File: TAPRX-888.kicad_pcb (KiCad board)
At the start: 6 copper layers, 76 x 100 mm, 222 parts, among them J1 CONN_SMA_JACK_RA, J10 U.FL-R, J11 Conn_JTAG10-mini, J2 CONN_SMA_JACK_RA, J3 CONN_SMA_JACK_RA, J4 CONN_SMA_JACK_RA, J5 USB-3.0, J6 Conn_01x03, J7 Conn_01x03, J8 Conn_01x03, J9 Conn_01x03, Q1 PMOS Si2343DS, Q2 MMBT3904, Q3 PMOS Si2343DS, U1 AP2114H-3.3TRG1, U10 XO-19.2MHZ, U11 CYUSB3014-BZXCT, U14 LP5907MFX-3.3, U16 TLV3501, U18 NC7SV157, U19 74LVC2G14, U2 AP2114H-3.3TRG1, U20 Si5351A, U21 NC7SV157, U22 SN65LVDS1, U3 AP2114H-3.3TRG1, U4 LP5907MFX-3.3, U5 UMW AMS1117-1.2, U6 AD8370, U7 TVS-SP3011, U8 LTC2208CUP_PBF, U9 MX25L3233FM2I, X1 TCXO-27M

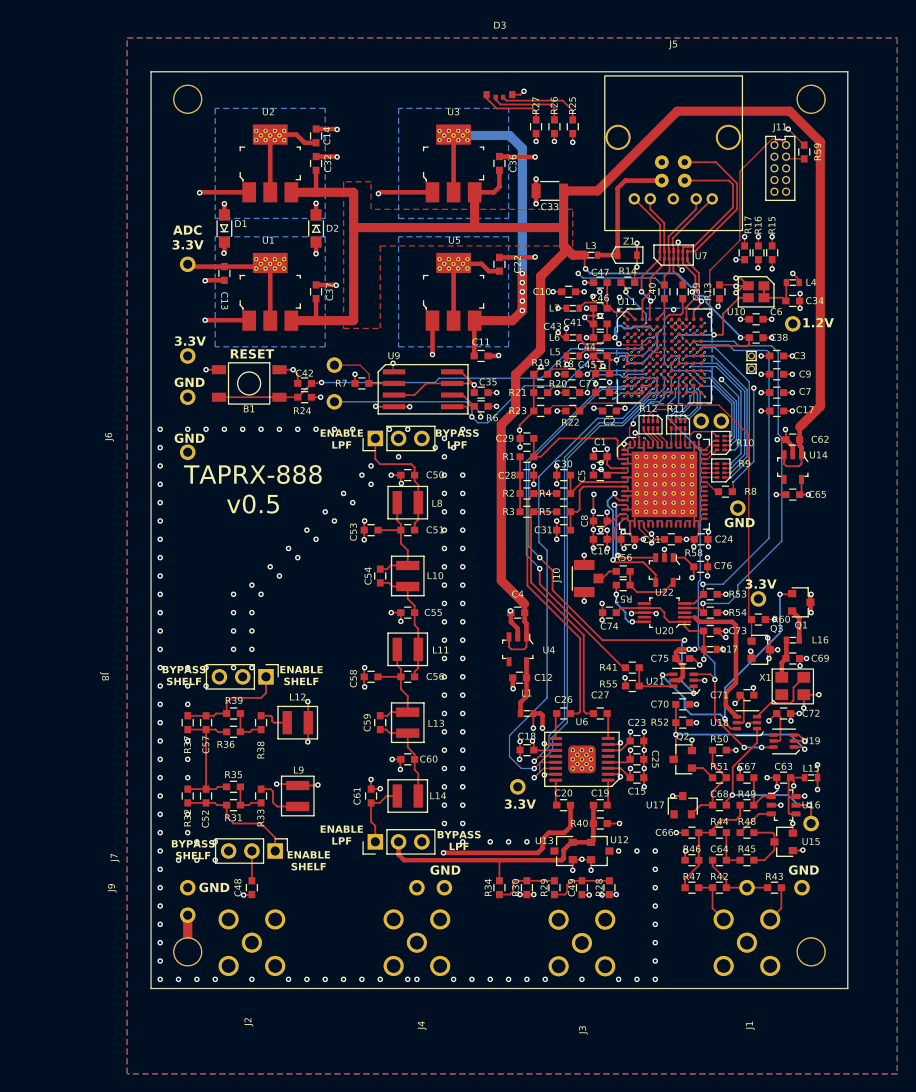
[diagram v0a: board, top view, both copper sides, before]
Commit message: Swap in newest design from TAPR/TAPRx888 c01bece; re-graft repo infra
The authoritative HF-SDR design was updated by the hardware designer on
TAPR/TAPRx888 (commit c01bece "proper update", Turn Island Systems). That
branch sits on the pre-flatten layout and also carried a stray
"TAPRX-888 KiCad - Copy/" duplicate + editor lock files, so a plain
cherry-pick was impossible. This lands only the real design edits, mapped
onto ringof's flattened root, and re-applies ringof's infra on top.

Design content taken verbatim from c01bece (mapped to repo root):
  - TAPRX-888.kicad_pcb   (layout/routing/net updates)
  - TAPRX-888.kicad_sch   (root schematic)
  - refclk.kicad_sch      (reference-clock sheet)
  - Library.kicad_sym     (symbol tweak)
  - TAPRX-888.kicad_pro   (used_designators, GIT_HASH text variable)

New file:
  - dru-not-included/TAPRX-888.kicad_dru — USB3 SuperSpeed / USB2 diff-pair
    DRC rules (skew, coupling, via limits, TX-RX isolation). Kept in a
    non-auto-loaded folder to preserve the designer's "not included" intent;
    move to repo root as TAPRX-888.kicad_dru to activate.

Infra re-grafted so nothing ringof added is lost:
  - (title_block) re-added to root/Front_End/refclk schematics + PCB, wired
    to the TAPR.kicad_wks worksheet via page_layout_descr_file in .kicad_pro.
  - Front_End.kicad_sch keeps its title block (designer did not touch it).

Dropped: the committed "Commit: ${GIT_HASH}" silkscreen gr_text on the PCB
(placeholder value; provenance is injected at build time per CLAUDE.md).
The GIT_HASH board property and .kicad_pro text variable remain as the
injection hook.

Co-Authored-By: Claude Opus 4.8 <noreply@anthropic.com>
Claude-Session: https://claude.ai/code/session_019A4jkTeNPLki8CdfTWEUwM
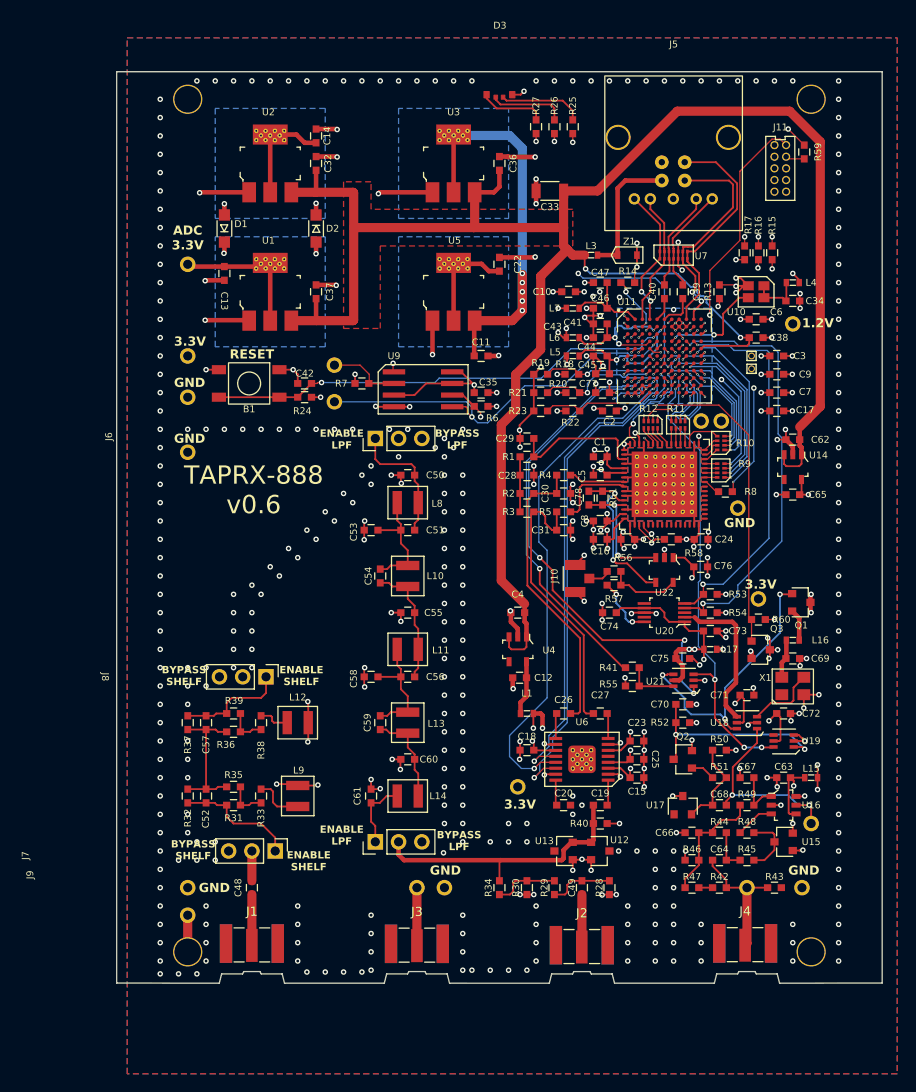
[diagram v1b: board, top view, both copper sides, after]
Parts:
- added C78: C-8.2p-0603, TIS_Footprints:PAD_0603, F.Cu at (147.8, 96.5)
- added G***: LOGO, TIS_Footprints:HamSCI-25mm, B.Cu at (118.5, 121.0)
- added R61: R-100-0603, TIS_Footprints:PAD_0603, F.Cu at (149.2, 96.5)
- J1, J2, J3, J4: value CONN_SMA_JACK_RA -> CONN_SMA_JACK_EDGE_JLC_With_Nut; footprint TIS_Footprints:SMA-RA-Jack -> TIS_Footprints:SMA_Jack_EdgeMount_JLC_With_Nut
- U8: value LTC2208CUP_PBF -> LTC2208CUP#PBF
- moved J1 54.0 mm to (111.0, 145.4), turned to 180 degrees
- moved J2 36.0 mm to (147.0, 145.6), turned to 180 degrees
- moved J4 35.8 mm to (164.8, 145.4), turned to 180 degrees
- moved J3 18.0 mm to (129.0, 145.4), turned to 180 degrees
- moved C30 2.00 mm to (145.0, 96.0), turned to 0 degrees
- moved R4 2.00 mm to (145.0, 94.0)
- moved R56 1.00 mm to (150.5, 104.5)
- moved R57 1.00 mm to (150.5, 106.0)
- moved J10 0.99 mm to (147.0, 105.3)
- turned C31 to 0 degrees
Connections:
- C30 pad 1: Net-(U8-AIN+) -> Net-(C26-Pad2)
- C31 pad 1: Net-(U8-AIN-) -> Net-(C27-Pad2)
- J1 pad 1: /Clock/EXT_REF_IN -> /Front_End_Filter/RF_IN
- J2 pad 1: /Front_End_Filter/RF_IN -> /Front_End_Filter/RF_ATTEN__IN
- J3 pad 1: /Front_End_Filter/RF_ATTEN__IN -> Net-(J3-In)
- J4 pad 1: Net-(J4-In) -> /Clock/EXT_REF_IN
- TP1 pad 1: Net-(J4-In) -> Net-(J3-In)
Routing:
- net GND: track 268.8 -> 242.0 mm, vias 326 -> 453
- net Net-(J3-In): track 0.00 -> 6.32 mm
- net Net-(J4-In): track 6.00 -> 0.00 mm
- net Net-(C27-Pad2): track 27.9 -> 31.2 mm
- net /SAMPLE_CLK_N: track 10.9 -> 13.7 mm
- net /SAMPLE_CLK_P: track 15.5 -> 17.9 mm
- net Net-(U8-AIN+): track 8.37 -> 6.16 mm
- net Net-(C26-Pad2): track 30.1 -> 32.1 mm
- net Net-(U8-AIN-): track 10.2 -> 8.56 mm
- net Net-(R56-Pad2): track 6.95 -> 7.95 mm
- net Net-(J10-In): track 1.85 -> 2.51 mm
- net /Front_End_Filter/RF_ATTEN__IN: track 6.32 -> 5.73 mm, vias 1 -> 0
- net /Front_End_Filter/RF_IN: track 6.42 -> 6.16 mm, vias 1 -> 0
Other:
- board size 76 x 100 mm -> 83.5 x 99.4 mm
- board text added: "Note: SMA connectors extend 0.6mm from board edge, 99.4mm + 0.6mm = 100mm"
- board text added: "TAPRX-888 v0.6"
- board text removed: "Commit: ${GIT_HASH}"
- board text removed: "TAPRX-888 v0.5"

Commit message: Restore GIT_HASH silkscreen and activate the DRU
Per design-owner direction, reverse the two infra decisions from the prior
commit:

- Restore the designer's "Commit: ${GIT_HASH}" silkscreen gr_text on the PCB
  (B.SilkS), verbatim from c01bece. The PCB now equals Paul's c01bece content
  differing only by the re-grafted (title_block).
- Activate the design rules: move dru-not-included/TAPRX-888.kicad_dru to the
  repo root as TAPRX-888.kicad_dru so KiCad auto-loads it during DRC
  (USB3 SuperSpeed / USB2 diff-pair skew, coupling, via limits, TX-RX
  isolation).

Co-Authored-By: Claude Opus 4.8 <noreply@anthropic.com>
Claude-Session: https://claude.ai/code/session_019A4jkTeNPLki8CdfTWEUwM
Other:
- board text added: "Commit: ${GIT_HASH}"
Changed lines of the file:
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@@
+		)
+	)
+	(gr_text "Commit: ${GIT_HASH}"
+		(at 129.9 131.2 0)
+		(layer "B.SilkS" knockout)
+		(effects
+			(font
+				(size 1.5 1.5)
+				(thickness 0.3)
+				(bold yes)
+			)
+			(justify left bottom mirror)
 		)
 	)
